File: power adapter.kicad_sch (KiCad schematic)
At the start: 6 parts

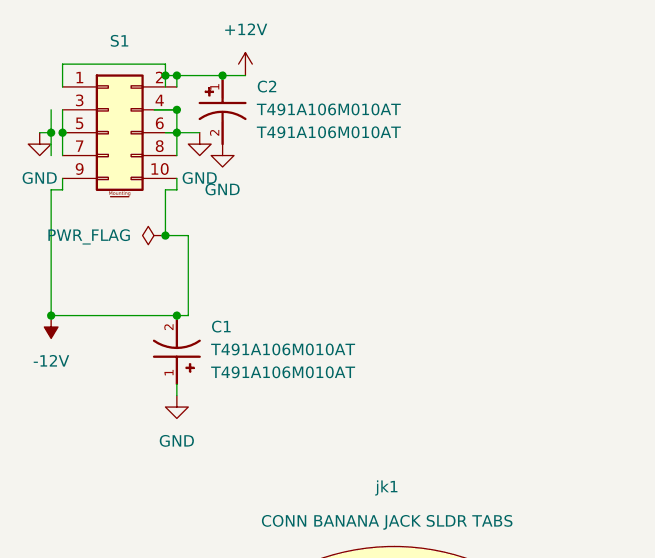
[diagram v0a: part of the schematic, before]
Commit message: added caps to power header
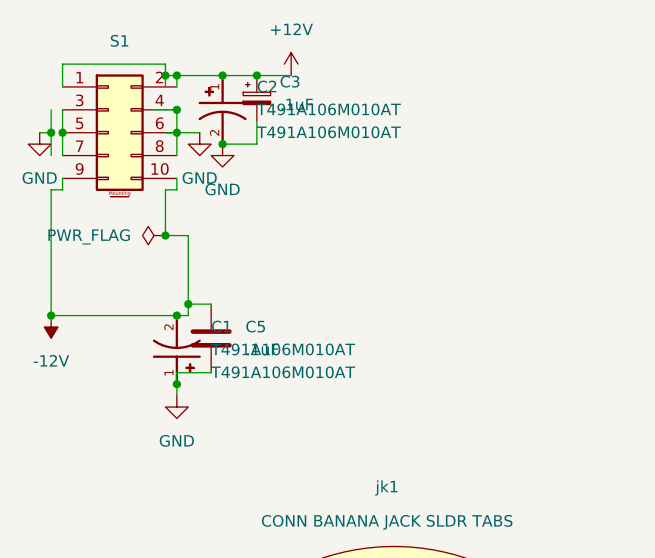
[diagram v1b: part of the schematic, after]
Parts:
- added C3: .1uF, symbol Device:C_Polarized_Small
- added C5: .1uF, Capacitor_SMD:C_0603_1608Metric, symbol Device:C
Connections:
- net +12V: now also C3.1
- net -12V: now also C5.1
- net GND: now also C3.2, C5.2
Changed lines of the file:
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@@
+	)
+	(junction
+		(at 35.56 71.12)
+		(diameter 0)
+		(color 0 0 0 0)
+	)
+	(junction
+		(at 40.64 44.45)
+		(diameter 0)
+		(color 0 0 0 0)
 	)
 	(junction
@@
 	)
 	(junction
+		(at 36.83 62.23)
+		(diameter 0)
+		(color 0 0 0 0)
+	)
+	(junction
+		(at 44.45 36.83)
+		(diameter 0)
+		(color 0 0 0 0)
+	)
+	(junction
 		(at 35.56 43.18)
 		(diameter 0)
@@
 	(wire
 		(pts
-			(xy 36.83 63.5) (xy 36.83 54.61)
+			(xy 36.83 63.5) (xy 36.83 62.23)
+		)
+		(stroke
+			(width 0)
+			(type default)
+		)
+	)
+	(wire
+		(pts
+			(xy 44.45 44.45) (xy 40.64 44.45)
 		)
 		(stroke
@@
 	(wire
 		(pts
+			(xy 36.83 62.23) (xy 39.37 62.23)
+		)
+		(stroke
+			(width 0)
+			(type default)
+		)
+	)
+	(wire
+		(pts
 			(xy 34.29 36.83) (xy 34.29 38.1)
 		)
@@
 	(wire
 		(pts
+			(xy 44.45 36.83) (xy 40.64 36.83)
+		)
+		(stroke
+			(width 0)
+			(type default)
+		)
+	)
+	(wire
+		(pts
 			(xy 22.86 38.1) (xy 22.86 35.56)
 		)
@@
 	(wire
 		(pts
-			(xy 43.18 36.83) (xy 40.64 36.83)
+			(xy 48.26 36.83) (xy 44.45 36.83)
 		)
 		(stroke
@@
 	(wire
 		(pts
-			(xy 35.56 72.39) (xy 35.56 71.12)
-		)
-		(stroke
-			(width 0)
-			(type default)
-		)
-	)
-	(wire
-		(pts
 			(xy 22.86 48.26) (xy 22.86 49.53)
 		)
@@
 	(wire
 		(pts
+			(xy 35.56 69.85) (xy 35.56 71.12)
+		)
+		(stroke
+			(width 0)
+			(type default)
+		)
+	)
+	(wire
+		(pts
+			(xy 44.45 41.91) (xy 44.45 44.45)
+		)
+		(stroke
+			(width 0)
+			(type default)
+		)
+	)
+	(wire
+		(pts
+			(xy 36.83 62.23) (xy 36.83 54.61)
+		)
+		(stroke
+			(width 0)
+			(type default)
+		)
+	)
+	(wire
+		(pts
 			(xy 35.56 36.83) (xy 35.56 38.1)
 		)
@@
 	(wire
 		(pts
+			(xy 35.56 71.12) (xy 35.56 72.39)
+		)
+		(stroke
+			(width 0)
+			(type default)
+		)
+	)
+	(wire
+		(pts
 			(xy 22.86 43.18) (xy 22.86 45.72)
+		)
+		(stroke
+			(width 0)
+			(type default)
+		)
+	)
+	(wire
+		(pts
+			(xy 39.37 69.85) (xy 35.56 69.85)
 		)
 		(stroke
@@
 	)
 	(symbol
+		(lib_id "Device:C")
+		(at 39.37 66.04 0)
+		(unit 1)
+		(exclude_from_sim no)
+		(in_bom yes)
+		(on_board yes)
+		(dnp no)
+		(fields_autoplaced yes)
+		(property "Reference" "C5"
+			(at 43.18 64.7699 0)
+			(effects
+				(font
+					(size 1.27 1.27)
+				)
+				(justify left)
+			)
+		)
+		(property "Value" ".1uF"
+			(at 43.18 67.3099 0)
+			(effects
+				(font
+					(size 1.27 1.27)
+				)
+				(justify left)
+			)
+		)
+		(property "Footprint" "Capacitor_SMD:C_0603_1608Metric"
+			(at 40.3352 69.85 0)
+			(effects
+				(font
+					(size 1.27 1.27)
+				)
+				(hide yes)
+			)
+		)
+		(property "Datasheet" "~"
+			(at 39.37 66.04 0)
+			(effects
+				(font
+					(size 1.27 1.27)
+				)
+				(hide yes)
+			)
+		)
+		(property "Description" "Unpolarized capacitor"
+			(at 39.37 66.04 0)
+			(effects
+				(font
+					(size 1.27 1.27)
+				)
+				(hide yes)
+			)
+		)
+		(pin "2"
+		)
+		(pin "1"
+		)
+		(instances
+			(project ""
+				(path "/91d95850-e011-4872-8c18-f0f818ae8f1c"
+					(reference "C5")
+					(unit 1)
+				)
+			)
+		)
+	)
+	(symbol
 		(lib_id "power:GND")
 		(at 38.1 43.18 0)
@@
 	(symbol
 		(lib_id "power:+12V")
-		(at 43.18 36.83 0)
+		(at 48.26 36.83 0)
 		(unit 1)
 		(exclude_from_sim no)
@@
 		(fields_autoplaced yes)
 		(property "Reference" "#PWR7"
-			(at 43.18 40.64 0)
+			(at 48.26 40.64 0)
 			(effects
 				(font
@@
 		)
 		(property "Value" "+12V"
-			(at 43.18 31.75 0)
+			(at 48.26 31.75 0)
 			(effects
 				(font
@@
 		)
 		(property "Footprint" ""
-			(at 43.18 36.83 0)
+			(at 48.26 36.83 0)
 			(effects
 				(font
@@
 		)
 		(property "Datasheet" ""
-			(at 43.18 36.83 0)
+			(at 48.26 36.83 0)
 			(effects
 				(font
@@
 		)
 		(property "Description" "Power symbol creates a global label with name \"+12V\""
-			(at 43.18 36.83 0)
+			(at 48.26 36.83 0)
 			(effects
 				(font
@@
 					(unit 1)
 				)
+			)
+		)
+	)
+	(symbol
+		(lib_id "Device:C_Polarized_Small")
+		(at 44.45 39.37 0)
+		(unit 1)
+		(exclude_from_sim no)
+		(in_bom yes)
+		(on_board yes)
+		(dnp no)
+		(fields_autoplaced yes)
+		(property "Reference" "C3"
+			(at 46.99 37.5538 0)
+			(effects
+				(font
+					(size 1.27 1.27)
+				)
+				(justify left)
+			)
+		)
+		(property "Value" ".1uF"
+			(at 46.99 40.0938 0)
+			(effects
+				(font
+					(size 1.27 1.27)
+				)
+				(justify left)
+			)
+		)
+		(property "Footprint" ""
+			(at 44.45 39.37 0)
+			(effects
+				(font
+					(size 1.27 1.27)
+				)
+				(hide yes)
+			)
+		)
+		(property "Datasheet" "~"
+			(at 44.45 39.37 0)
+			(effects
+				(font
+					(size 1.27 1.27)
+				)
+				(hide yes)
+			)
+		)
+		(property "Description" "Polarized capacitor, small symbol"
+			(at 44.45 39.37 0)
+			(effects
+				(font
+					(size 1.27 1.27)
+				)
+				(hide yes)
+			)
+		)
+		(pin "1"
+		)
+		(pin "2"
+		)
+		(instances
+			(project ""
+				(path "/91d95850-e011-4872-8c18-f0f818ae8f1c"
+					(reference "C3")
+					(unit 1)
+				)

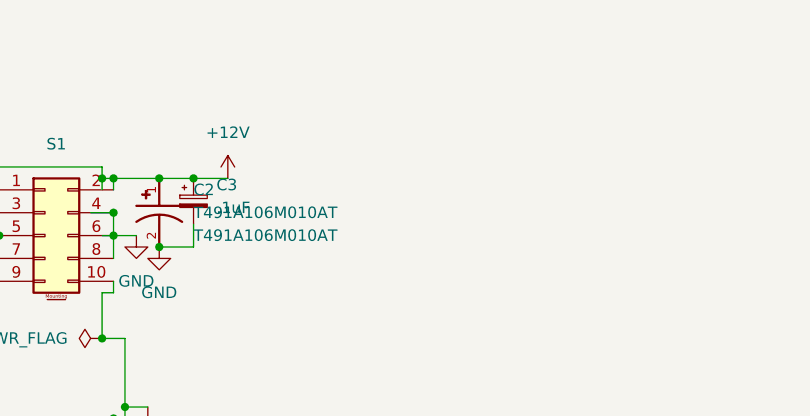
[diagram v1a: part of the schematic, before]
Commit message: added my golden test resistor and updated symbol and footprint directories in paths
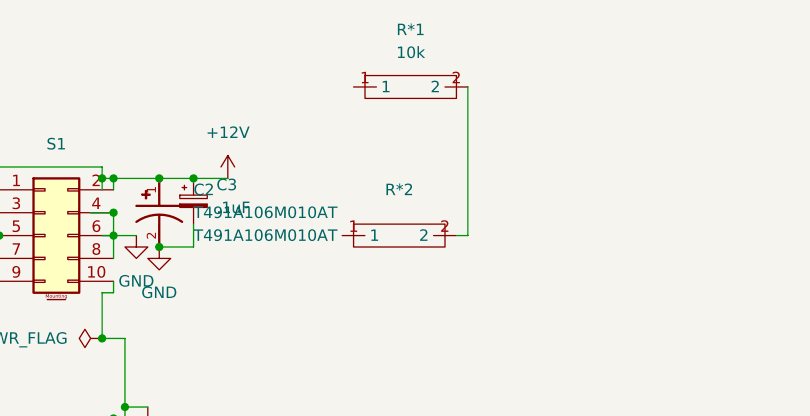
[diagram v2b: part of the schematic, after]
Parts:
- added R*1: 10k, commonfootprint:Modcan0603, symbol common:R
- added R*2: ~, commonfootprint:Modcan0603, symbol common:R
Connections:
- new net: R*1.2, R*2.2
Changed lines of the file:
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@@
+	(wire
+		(pts
+			(xy 74.93 43.18) (xy 73.66 43.18)
+		)
+		(stroke
+			(width 0)
+			(type default)
+		)
+	)
 	(wire
 		(pts
@@
 		(pts
 			(xy 35.56 71.12) (xy 35.56 72.39)
+		)
+		(stroke
+			(width 0)
+			(type default)
+		)
+	)
+	(wire
+		(pts
+			(xy 74.93 26.67) (xy 74.93 43.18)
 		)
 		(stroke
@@
 					(unit 1)
 				)
+			)
+		)
+	)
+	(symbol
+		(lib_id "common:R")
+		(at 68.58 25.4 0)
+		(unit 1)
+		(exclude_from_sim no)
+		(in_bom yes)
+		(on_board yes)
+		(dnp no)
+		(fields_autoplaced yes)
+		(property "Reference" "R*1"
+			(at 68.58 20.32 0)
+			(effects
+				(font
+					(size 1.27 1.27)
+				)
+			)
+		)
+		(property "Value" "10k"
+			(at 68.58 22.86 0)
+			(effects
+				(font
+					(size 1.27 1.27)
+				)
+			)
+		)
+		(property "Footprint" "commonfootprint:Modcan0603"
+			(at 68.58 25.4 0)
+			(effects
+				(font
+					(size 1.27 1.27)
+				)
+				(hide yes)
+			)
+		)
+		(property "Datasheet" ""
+			(at 68.58 25.4 0)
+			(effects
+				(font
+					(size 1.27 1.27)
+				)
+				(hide yes)
+			)
+		)
+		(property "Description" ""
+			(at 68.58 25.4 0)
+			(effects
+				(font
+					(size 1.27 1.27)
+				)
+				(hide yes)
+			)
+		)
+		(pin "2"
+		)
+		(pin "1"
+		)
+		(instances
+			(project ""
+				(path "/91d95850-e011-4872-8c18-f0f818ae8f1c"
+					(reference "R*1")
+					(unit 1)
+				)
+			)
+		)
+	)
+	(symbol
+		(lib_id "common:R")
+		(at 67.31 41.91 0)
+		(unit 1)
+		(exclude_from_sim no)
+		(in_bom yes)
+		(on_board yes)
+		(dnp no)
+		(fields_autoplaced yes)
+		(property "Reference" "R*2"
+			(at 67.31 38.1 0)
+			(effects
+				(font
+					(size 1.27 1.27)
+				)
+			)
+		)
+		(property "Value" "~"
+			(at 67.31 40.64 0)
+			(effects
+				(font
+					(size 1.27 1.27)
+				)
+			)
+		)
+		(property "Footprint" "commonfootprint:Modcan0603"
+			(at 67.31 41.91 0)
+			(effects
+				(font
+					(size 1.27 1.27)
+				)
+				(hide yes)
+			)
+		)
+		(property "Datasheet" ""
+			(at 67.31 41.91 0)
+			(effects
+				(font
+					(size 1.27 1.27)
+				)
+				(hide yes)
+			)
+		)
+		(property "Description" ""
+			(at 67.31 41.91 0)
+			(effects
+				(font
+					(size 1.27 1.27)
+				)
+				(hide yes)
+			)
+		)
+		(pin "2"
+		)
+		(pin "1"
+		)
+		(instances
+			(project ""
+				(path "/91d95850-e011-4872-8c18-f0f818ae8f1c"
+					(reference "R*2")
+					(unit 1)
+				)
